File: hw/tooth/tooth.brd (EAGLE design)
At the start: 10.5 x 10.5 mm, 24 parts, among them X1 416F32022CKR

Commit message: hw: Add serial number of chip used on prototypes
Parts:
- IC2: value (none) -> N52832 CIAAB0
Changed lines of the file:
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@@
 </element>
 <element name="U$2" library="smartwatch" package="SC75_INFINEON" value="SI1013" x="2" y="-3.58" rot="R270"/>
-<element name="IC2" library="dan" package="NRF52832_WLCSP" value="" x="-3.23" y="0.25" rot="R270"/>
+<element name="IC2" library="dan" package="NRF52832_WLCSP" value="N52832 CIAAB0" x="-3.23" y="0.25" rot="R270"/>
 <element name="C1" library="rcl" package="C0201" value="12pF" x="3.93" y="1.26" rot="R90"/>
 <element name="C2" library="rcl" package="C0201" value="12pF" x="1.61" y="1.38" rot="R270"/>

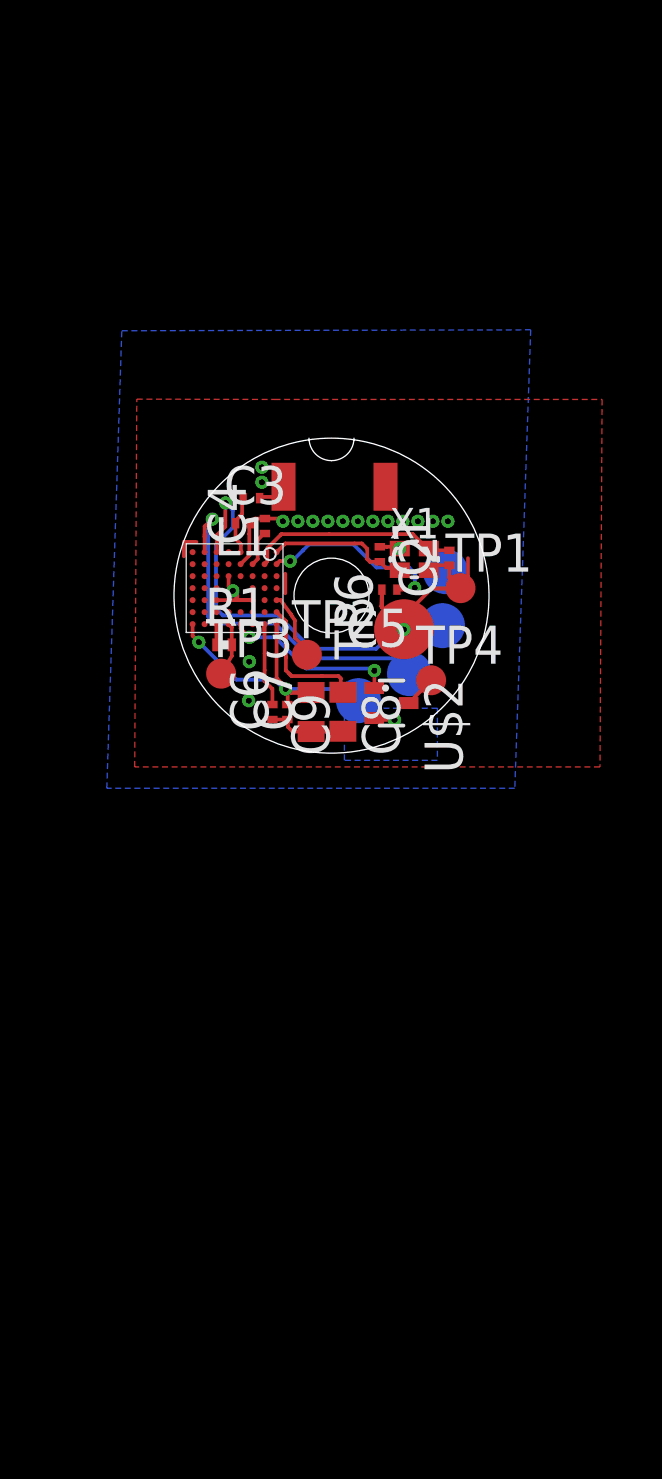
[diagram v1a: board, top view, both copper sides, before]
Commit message: hw: Add new, smaller board revision
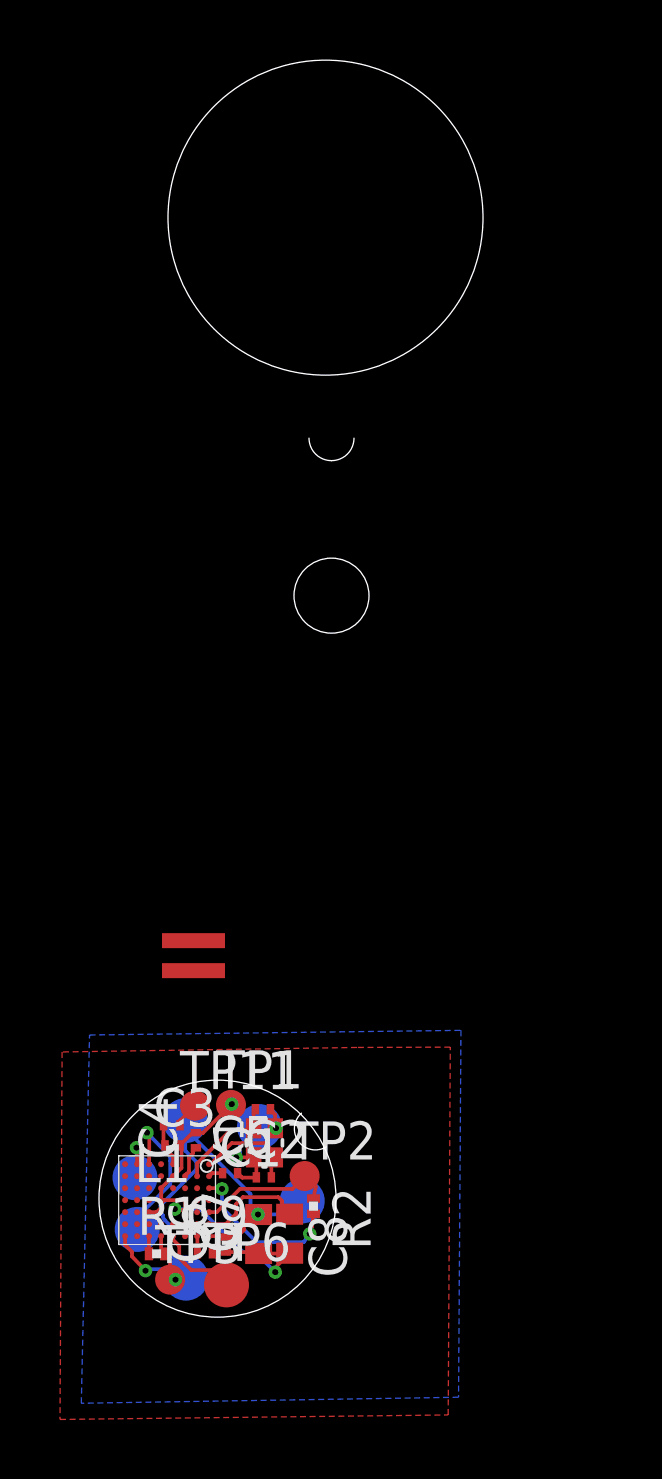
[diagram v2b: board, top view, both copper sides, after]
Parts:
- removed TP4: TPTP10R, testpad:TP10R
- removed U$2: SI1013, smartwatch:SC75_INFINEON
- removed U$3: 2450AT18A100, dan:2450AT18A100
- added R2: 33K, rcl:R0201
- added TP11: TPTP10R, testpad:TP10R
- added TP12, TP5: TPTP15R, testpad:TP15R
- added U$1: ACA-102-T, dan:ACA-102-T
- IC2: value N52832 CIAAB0 -> (none)
- TP6: value TPTP20R -> TPTP15R; device testpad:TP20R -> testpad:TP15R
- moved TP6 22.6 mm to (-3.50, -23.0), turned to 0 degrees
- moved TP9 22.6 mm to (-6.47, -21.1)
- moved C2 21.1 mm to (-2.25, -19.4), turned to 0 degrees
- moved L1 21.1 mm to (-5.33, -17.6)
- moved C3 20.9 mm to (-5.30, -18.3)
- moved C4 20.6 mm to (-4.52, -18.2)
- moved IC2 20.5 mm to (-5.48, -20.1)
- moved R1 20.4 mm to (-5.83, -21.9)
- moved TP3 20.3 mm to (-5.38, -22.8)
- moved C5 20.2 mm to (-3.38, -19.2), turned to 0 degrees
- moved TP7 20.1 mm to (-4.85, -22.8)
- moved X1 20.1 mm to (-2.23, -18.2), turned to 90 degrees
- moved TP10 19.5 mm to (-2.40, -17.7)
- moved C1 19.4 mm to (-2.29, -17.1), turned to 180 degrees
- moved TP8 19.1 mm to (-6.55, -19.4)
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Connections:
- removed net AIN4: IC2.A3
- removed net N$13: L1.1, U$3.P$1
- removed net N$5: TP4.TP, U$2.3
- new net N$3: L1.1, TP11.TP
- new net PHON: IC2.A3, R2.2
- net 3.3V: now also TP12.TP, TP5.TP; no longer U$2.2
- net AIN6: now also R2.1
- net GND: no longer TP6.TP
- net SON: now also TP6.TP; no longer U$2.1
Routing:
- net SWDIO: track 12.2 -> 1.82 mm
- net SWDCLK: track 14.3 -> 5.12 mm
- net N$10: track 6.45 -> 0.49 mm, vias 2 -> 0
- net PHON: track 0.00 -> 5.29 mm, vias 0 -> 2
- net 3.3V: track 14.6 -> 19.5 mm
- net N$6: track 7.03 -> 3.45 mm
- net SON: track 5.78 -> 3.03 mm, vias 2 -> 0
- net N$19: track 3.07 -> 0.57 mm
- net AIN6: track 2.27 -> 4.66 mm
- net GND: track 19.1 -> 21.4 mm, vias 19 -> 5
- net N$2: track 4.79 -> 3.48 mm
- net N$13: track 1.18 -> 0.00 mm
- net N$5: track 1.07 -> 0.00 mm
- net N$7: track 0.65 -> 0.00 mm
- net N$3: track 0.36 -> 1.00 mm
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- removed copper zone on layer 16, net 3.3V
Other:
- board size 10.5 x 10.5 mm -> 12.8 x 41.9 mm

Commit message: hw: Clean-up design files
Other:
- board size 12.8 x 41.9 mm -> 7.9 x 7.9 mm
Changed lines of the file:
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@@
 <layer number="20" name="Dimension" color="15" fill="1" visible="yes" active="yes"/>
 <layer number="21" name="tPlace" color="7" fill="1" visible="yes" active="yes"/>
-<layer number="22" name="bPlace" color="7" fill="1" visible="no" active="yes"/>
+<layer number="22" name="bPlace" color="7" fill="1" visible="yes" active="yes"/>
 <layer number="23" name="tOrigins" color="15" fill="1" visible="yes" active="yes"/>
 <layer number="24" name="bOrigins" color="15" fill="1" visible="yes" active="yes"/>
@@
 <board>
 <plain>
-<circle x="-0.2" y="12.6" radius="5.25" width="0.01" layer="20"/>
-<rectangle x1="-1.86" y1="2.67" x2="4.06" y2="5.14" layer="41"/>
-<rectangle x1="-2.2" y1="2.52" x2="4" y2="5" layer="42"/>
-<wire x1="0" y1="4.5" x2="0.75" y2="5.25" width="0.01" layer="20" curve="90"/>
-<wire x1="0" y1="4.5" x2="-0.75" y2="5.25" width="0.01" layer="20" curve="-90"/>
-<polygon width="0.01" layer="30">
-<vertex x="3.88" y="-3.74"/>
-<vertex x="0.41" y="-3.74"/>
-<vertex x="0.41" y="-5.53"/>
-<vertex x="3.91" y="-5.53"/>
-<vertex x="3.91" y="-3.74"/>
-</polygon>
-<hole x="0" y="0" drill="2.5"/>
-<rectangle x1="-0.04" y1="-5.95" x2="0.43" y2="-2.9" layer="42"/>
 <circle x="-4.16" y="-19.01" radius="0.031621875" width="0.4064" layer="21"/>
-<wire x1="-14.7" y1="-13.4" x2="-14.7" y2="-7.4" width="0.1" layer="248"/>
-<wire x1="-14.7" y1="-7.4" x2="-12.7" y2="-7.4" width="0.1" layer="248"/>
-<wire x1="-12.7" y1="-7.4" x2="-12.7" y2="-13.4" width="0.1" layer="248"/>
-<wire x1="-12.7" y1="-13.4" x2="-14.7" y2="-13.4" width="0.1" layer="248"/>
-<wire x1="-10.2" y1="-13.4" x2="-10.2" y2="-7.4" width="0.1" layer="248"/>
-<wire x1="-10.2" y1="-7.4" x2="-8.2" y2="-7.4" width="0.1" layer="248"/>
-<wire x1="-8.2" y1="-7.4" x2="-8.2" y2="-13.4" width="0.1" layer="248"/>
-<wire x1="-8.2" y1="-13.4" x2="-10.2" y2="-13.4" width="0.1" layer="248"/>
-<circle x="-21.2" y="-11.3" radius="2.9" width="0.1" layer="248"/>
-<wire x1="-19" y1="-3" x2="-17.5" y2="-3" width="0.1" layer="248"/>
-<wire x1="-13.5" y1="-3" x2="-12" y2="-3" width="0.1" layer="248"/>
-<wire x1="-12" y1="-3" x2="-12" y2="3" width="0.1" layer="248"/>
-<wire x1="-12" y1="3" x2="-19" y2="3" width="0.1" layer="248"/>
-<wire x1="-19" y1="3" x2="-19" y2="-3" width="0.1" layer="248"/>
-<wire x1="-15" y1="-2.5" x2="-17" y2="-2.5" width="0.1" layer="248"/>
-<wire x1="-17" y1="-2.5" x2="-17.5" y2="-3" width="0.1" layer="248"/>
-<wire x1="-15" y1="-2.5" x2="-14" y2="-2.5" width="0.1" layer="248"/>
-<wire x1="-14" y1="-2.5" x2="-13.5" y2="-3" width="0.1" layer="248"/>
 <circle x="-3.8" y="-20.1" radius="3.95" width="0.01" layer="20"/>
-<circle x="9.2" y="-17.6" radius="4.75" width="0.1" layer="248"/>
 <wire x1="-0.175" y1="-18.375" x2="-1" y2="-17.25" width="0.01" layer="20" curve="-169.76"/>
 </plain>
